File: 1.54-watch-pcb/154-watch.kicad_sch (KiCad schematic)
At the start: 59 parts, among them J1 AFC24-S24FIC-00, J2 Conn_01x06_Female, J3 USB_C_Programming, J4 Jack-DC, J5 Conn_01x02_Male, Q1 Si1308, Q2 BC817, Q3 BC817, Q4 Si2301CDS, SW1 RESET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

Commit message: RX -> TX  should be always crossed
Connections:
- net RX: now also U3.17 (RXD); no longer U3.18 (TXD)
- net TX: now also U3.18 (TXD); no longer U3.17 (RXD)
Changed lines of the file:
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@@
+    )
+  )
+  (global_label "TX" (shape input) (at 323.85 64.77 180) (fields_autoplaced)
+    (effects (font (size 1.27 1.27)) (justify right))
+    (property "Intersheet References" "${INTERSHEET_REFS}" (id 0) (at 319.2598 64.8494 0)
+      (effects (font (size 1.27 1.27)) (justify right) hide)
     )
   )
@@
     (effects (font (size 1.27 1.27)) (justify right))
     (property "Intersheet References" "${INTERSHEET_REFS}" (id 0) (at 158.2721 199.3106 0)
-      (effects (font (size 1.27 1.27)) (justify right) hide)
-    )
-  )
-  (global_label "RX" (shape input) (at 323.85 64.77 180) (fields_autoplaced)
-    (effects (font (size 1.27 1.27)) (justify right))
-    (property "Intersheet References" "${INTERSHEET_REFS}" (id 0) (at 318.9574 64.8494 0)
       (effects (font (size 1.27 1.27)) (justify right) hide)
     )
@@
     )
   )
-  (global_label "TX" (shape input) (at 328.93 67.31 180) (fields_autoplaced)
-    (effects (font (size 1.27 1.27)) (justify right))
-    (property "Intersheet References" "${INTERSHEET_REFS}" (id 0) (at 324.3398 67.3894 0)
+  (global_label "RX" (shape input) (at 328.93 67.31 180) (fields_autoplaced)
+    (effects (font (size 1.27 1.27)) (justify right))
+    (property "Intersheet References" "${INTERSHEET_REFS}" (id 0) (at 324.0374 67.3894 0)
       (effects (font (size 1.27 1.27)) (justify right) hide)
     )
@@
       (effects (font (size 1.27 1.27)) hide)
     )
-    (property "Value" "GND" (id 1) (at 355.6 57.15 0))
+    (property "Value" "GND" (id 1) (at 359.41 59.69 0))
     (property "Footprint" "" (id 2) (at 359.41 55.88 0)
       (effects (font (size 1.27 1.27)) hide)

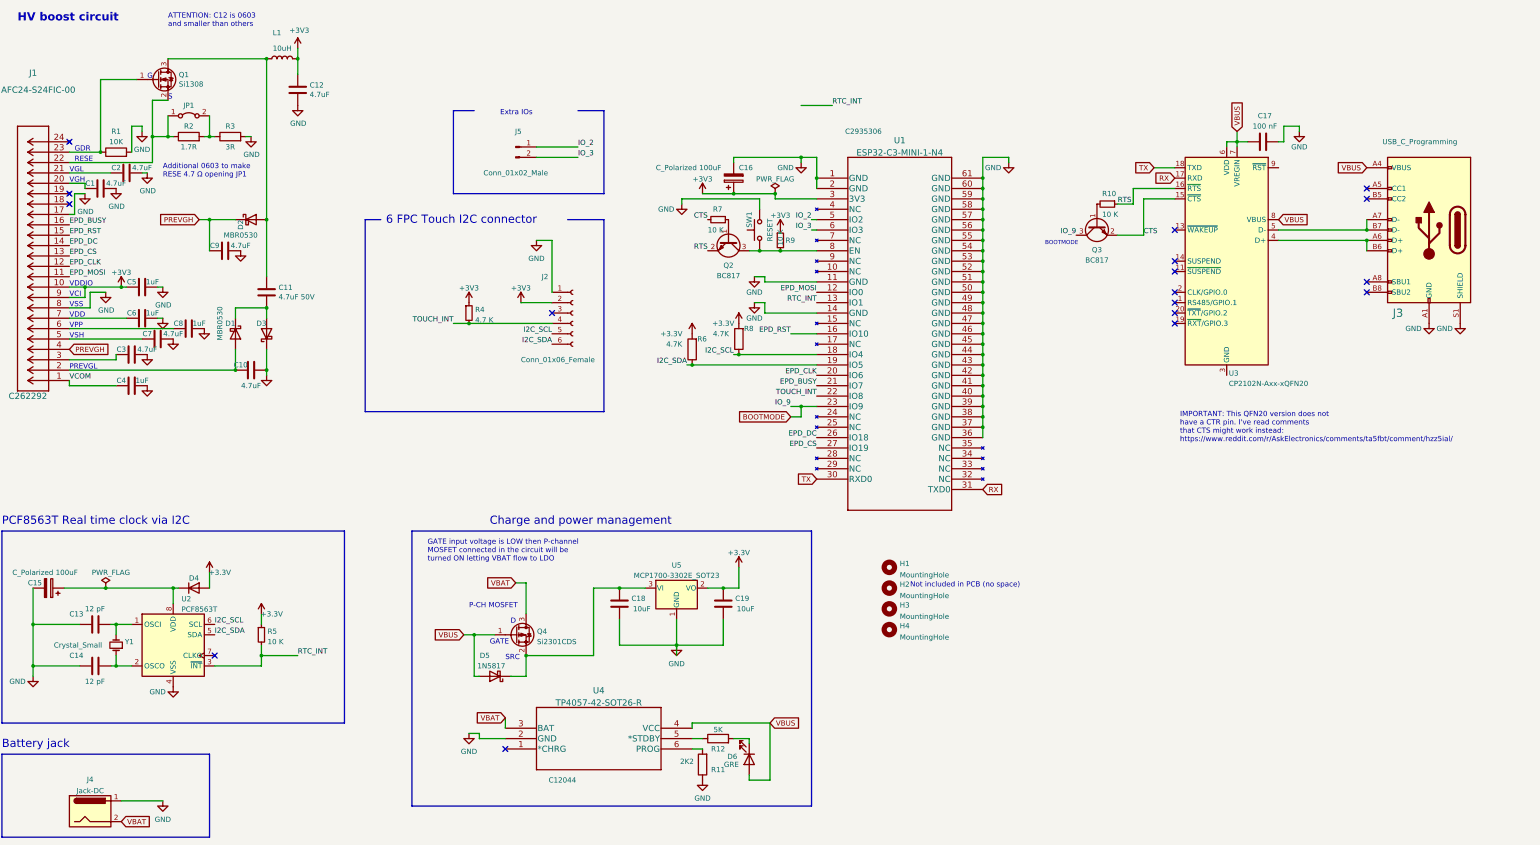
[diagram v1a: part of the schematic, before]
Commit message: #6 update 1.54" PCB to match sample sent by GOODISPLAY
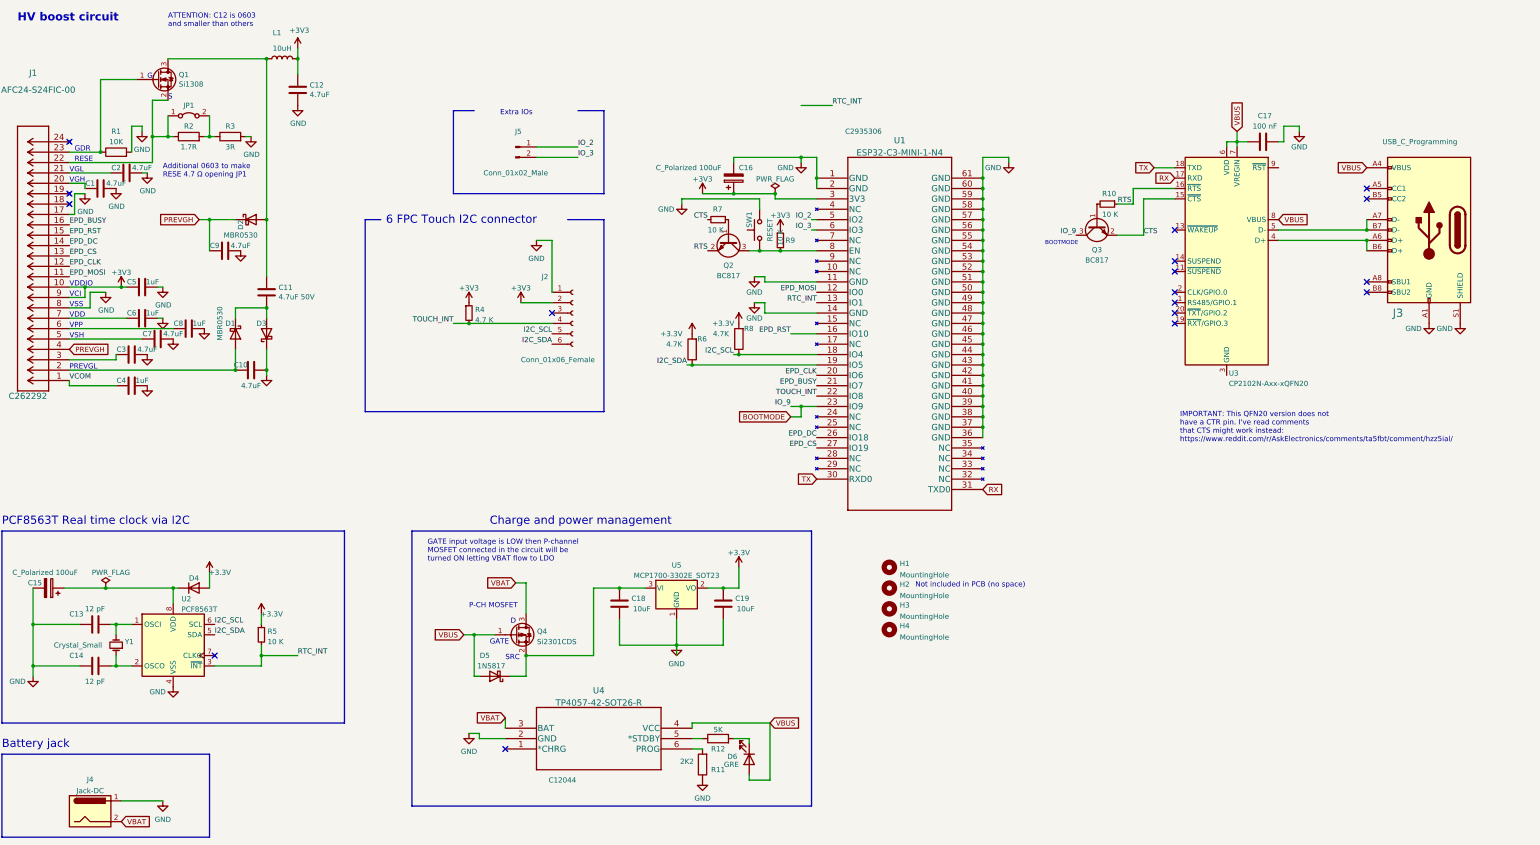
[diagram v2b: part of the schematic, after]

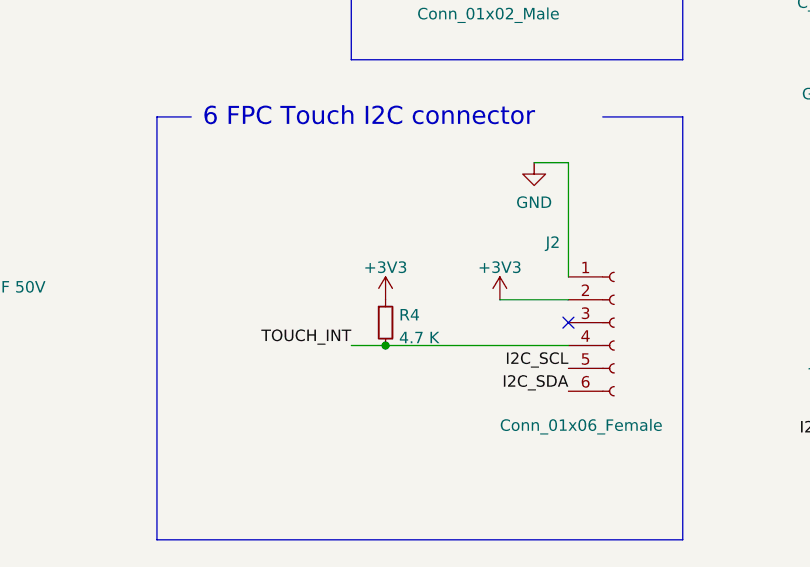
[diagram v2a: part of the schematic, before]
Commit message: #6 Update touch PINUP (Was wrong)
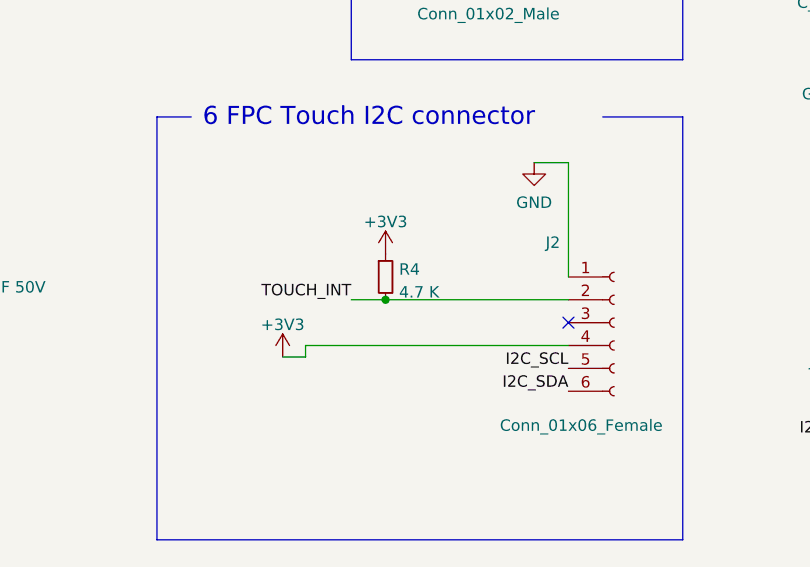
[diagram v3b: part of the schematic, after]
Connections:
- net +3V3: now also J2.4 (Pin_4); no longer J2.2 (Pin_2)
- net TOUCH_INT: now also J2.2 (Pin_2); no longer J2.4 (Pin_4)
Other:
- moved on the sheet: R4
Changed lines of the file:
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@@
   (junction (at 106.68 77.47) (diameter 0) (color 0 0 0 0)
   )
-  (junction (at 156.21 102.87) (diameter 0) (color 0 0 0 0)
-  )
   (junction (at 375.92 80.01) (diameter 0) (color 0 0 0 0)
   )
@@
   (junction (at 281.94 115.57) (diameter 0) (color 0 0 0 0)
   )
+  (junction (at 156.21 97.79) (diameter 0) (color 0 0 0 0)
+  )
   (no_connect (at 328.93 90.17))
   (no_connect (at 165.1 207.01))
@@
     (stroke (width 0) (type default))
   )
+  (wire (pts (xy 147.32 102.87) (xy 147.32 104.14))
+    (stroke (width 0) (type default))
+  )
   (polyline (pts (xy 41.91 153.67) (xy 41.91 200.66))
     (stroke (width 0) (type default))
@@
     (stroke (width 0) (type default))
   )
-  (wire (pts (xy 168.91 97.79) (xy 176.53 97.79))
-    (stroke (width 0) (type default))
-  )
   (wire (pts (xy 209.55 113.03) (xy 210.82 113.03))
     (stroke (width 0) (type default))
   )
-  (wire (pts (xy 156.21 102.87) (xy 176.53 102.87))
-    (stroke (width 0) (type default))
-  )
   (wire (pts (xy 375.92 82.55) (xy 375.92 85.09))
     (stroke (width 0) (type default))
@@
     (stroke (width 0) (type default))
   )
+  (wire (pts (xy 176.53 102.87) (xy 147.32 102.87))
+    (stroke (width 0) (type default))
+  )
   (wire (pts (xy 106.68 38.1) (xy 106.68 77.47))
     (stroke (width 0) (type default))
@@
     (stroke (width 0) (type default))
   )
-  (wire (pts (xy 152.4 102.87) (xy 156.21 102.87))
+  (wire (pts (xy 152.4 97.79) (xy 156.21 97.79))
     (stroke (width 0) (type default))
   )
@@
     (stroke (width 0) (type default))
   )
+  (wire (pts (xy 147.32 104.14) (xy 144.78 104.14))
+    (stroke (width 0) (type default))
+  )
   (wire (pts (xy 210.82 113.03) (xy 241.3 113.03))
     (stroke (width 0) (type default))
@@
     (stroke (width 0) (type default))
   )
+  (wire (pts (xy 156.21 97.79) (xy 176.53 97.79))
+    (stroke (width 0) (type default))
+  )
   (wire (pts (xy 210.82 200.66) (xy 210.82 201.93))
     (stroke (width 0) (type default))
@@
     (effects (font (size 1.27 1.27)) (justify left bottom))
   )
-  (label "TOUCH_INT" (at 152.4 102.87 180) (fields_autoplaced)
+  (label "TOUCH_INT" (at 152.4 97.79 180) (fields_autoplaced)
     (effects (font (size 1.27 1.27)) (justify right bottom))
   )
@@
     )
   )
-  (symbol (lib_id "power:+3V3") (at 168.91 97.79 0) (unit 1)
+  (symbol (lib_id "power:+3V3") (at 144.78 104.14 0) (unit 1)
     (in_bom yes) (on_board yes) (dnp no) (fields_autoplaced)
-    (property "Reference" "#PWR021" (at 168.91 101.6 0)
+    (property "Reference" "#PWR021" (at 144.78 107.95 0)
       (effects (font (size 1.27 1.27)) hide)
     )
-    (property "Value" "+3V3" (at 168.91 94.2142 0)
+    (property "Value" "+3V3" (at 144.78 100.5642 0)
       (effects (font (size 1.27 1.27)))
     )
-    (property "Footprint" "" (at 168.91 97.79 0)
+    (property "Footprint" "" (at 144.78 104.14 0)
       (effects (font (size 1.27 1.27)) hide)
     )
-    (property "Datasheet" "" (at 168.91 97.79 0)
+    (property "Datasheet" "" (at 144.78 104.14 0)
       (effects (font (size 1.27 1.27)) hide)
     )
@@
     )
   )
-  (symbol (lib_id "power:+3V3") (at 156.21 97.79 0) (unit 1)
+  (symbol (lib_id "power:+3V3") (at 156.21 92.71 0) (unit 1)
     (in_bom yes) (on_board yes) (dnp no) (fields_autoplaced)
-    (property "Reference" "#PWR05" (at 156.21 101.6 0)
+    (property "Reference" "#PWR05" (at 156.21 96.52 0)
       (effects (font (size 1.27 1.27)) hide)
     )
-    (property "Value" "+3V3" (at 156.21 94.2142 0)
+    (property "Value" "+3V3" (at 156.21 89.1342 0)
       (effects (font (size 1.27 1.27)))
     )
-    (property "Footprint" "" (at 156.21 97.79 0)
+    (property "Footprint" "" (at 156.21 92.71 0)
       (effects (font (size 1.27 1.27)) hide)
     )
-    (property "Datasheet" "" (at 156.21 97.79 0)
+    (property "Datasheet" "" (at 156.21 92.71 0)
       (effects (font (size 1.27 1.27)) hide)
     )
@@
     )
   )
-  (symbol (lib_id "Device:R_Small") (at 156.21 100.33 0) (unit 1)
+  (symbol (lib_id "Device:R_Small") (at 156.21 95.25 0) (unit 1)
     (in_bom yes) (on_board yes) (dnp no)
-    (property "Reference" "R4" (at 157.7086 99.4953 0)
+    (property "Reference" "R4" (at 157.7086 94.4153 0)
       (effects (font (size 1.27 1.27)) (justify left))
     )
-    (property "Value" "4.7 K" (at 157.7086 102.0322 0)
+    (property "Value" "4.7 K" (at 157.7086 96.9522 0)
       (effects (font (size 1.27 1.27)) (justify left))
     )
-    (property "Footprint" "Resistor_SMD:R_0603_1608Metric" (at 156.21 100.33 0)
+    (property "Footprint" "Resistor_SMD:R_0603_1608Metric" (at 156.21 95.25 0)
       (effects (font (size 1.27 1.27)) hide)
     )
-    (property "Datasheet" "https://jlcpcb.com/partdetail/23889-0603WAF4701T5E/C23162" (at 156.21 100.33 0)
+    (property "Datasheet" "https://jlcpcb.com/partdetail/23889-0603WAF4701T5E/C23162" (at 156.21 95.25 0)
       (effects (font (size 1.27 1.27)) hide)
     )
-    (property "LCSC" "C23162" (at 156.21 100.33 0)
+    (property "LCSC" "C23162" (at 156.21 95.25 0)
       (effects (font (size 1.27 1.27)) hide)
     )

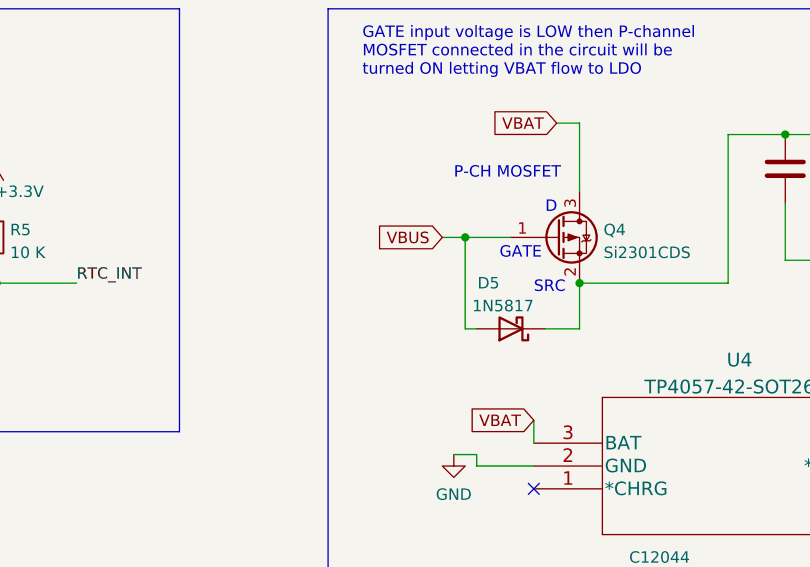
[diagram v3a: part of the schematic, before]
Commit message: #6 Add a pull-down to power switch Q4
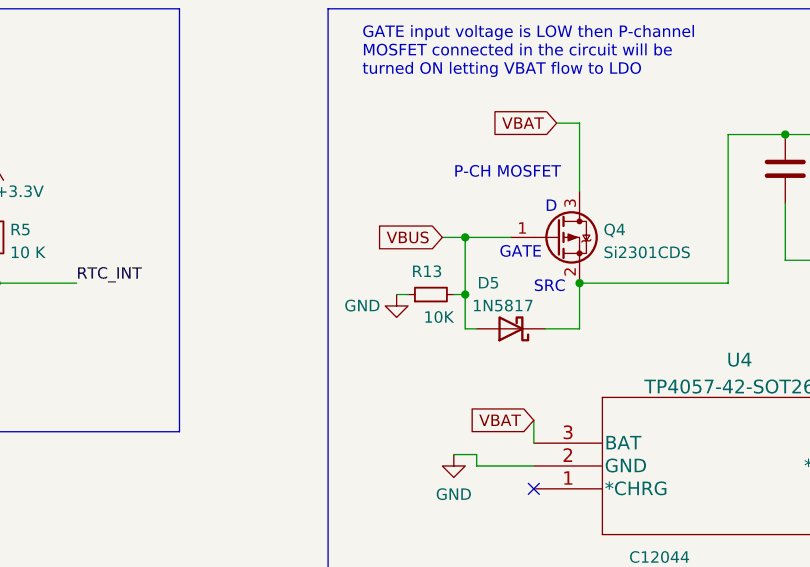
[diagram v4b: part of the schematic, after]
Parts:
- added R13: 10K, Resistor_SMD:R_0603_1608Metric, symbol Device:R_Small
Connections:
- net GND: now also R13.1
- net VBUS: now also R13.2
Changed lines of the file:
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@@
   (junction (at 281.94 100.33) (diameter 0) (color 0 0 0 0)
   )
+  (junction (at 157.48 185.42) (diameter 0) (color 0 0 0 0)
+  )
   (junction (at 71.12 93.98) (diameter 0) (color 0 0 0 0)
   )
@@
     (stroke (width 0) (type default))
   )
+  (wire (pts (xy 156.21 185.42) (xy 157.48 185.42))
+    (stroke (width 0) (type default))
+  )
   (wire (pts (xy 228.6 92.71) (xy 228.6 91.44))
     (stroke (width 0) (type default))
@@
     (stroke (width 0) (type default))
   )
-  (wire (pts (xy 157.48 179.07) (xy 157.48 189.23))
+  (wire (pts (xy 157.48 179.07) (xy 157.48 185.42))
     (stroke (width 0) (type default))
   )
@@
     (stroke (width 0) (type default))
   )
+  (wire (pts (xy 149.86 185.42) (xy 151.13 185.42))
+    (stroke (width 0) (type default))
+  )
   (wire (pts (xy 227.33 74.93) (xy 227.33 72.39))
     (stroke (width 0) (type default))
@@
     (stroke (width 0) (type default))
   )
+  (wire (pts (xy 157.48 185.42) (xy 157.48 189.23))
+    (stroke (width 0) (type default))
+  )
   (wire (pts (xy 359.41 54.61) (xy 359.41 55.88))
     (stroke (width 0) (type default))
@@
     )
   )
+  (symbol (lib_id "power:GND") (at 149.86 185.42 0) (unit 1)
+    (in_bom yes) (on_board yes) (dnp no)
+    (property "Reference" "#PWR034" (at 149.86 191.77 0)
+      (effects (font (size 1.27 1.27)) hide)
+    )
+    (property "Value" "GND" (at 146.05 186.69 0)
+      (effects (font (size 1.27 1.27)))
+    )
+    (property "Footprint" "" (at 149.86 185.42 0)
+      (effects (font (size 1.27 1.27)) hide)
+    )
+    (property "Datasheet" "" (at 149.86 185.42 0)
+      (effects (font (size 1.27 1.27)) hide)
+    )
+    (pin "1")
+    (instances
+      (project "154-watch"
+        (path "/ea6fde00-59dc-4a79-a647-7e38199fae0e"
+          (reference "#PWR034") (unit 1)
+        )
+      )
+    )
+  )
   (symbol (lib_id "power:GND") (at 77.47 110.49 0) (unit 1)
     (in_bom yes) (on_board yes) (dnp no)
@@
         )
       )
+    )
+  )
+  (symbol (lib_id "Device:R_Small") (at 153.67 185.42 90) (unit 1)
+    (in_bom yes) (on_board yes) (dnp no)
+    (property "Reference" "R13" (at 154.94 182.88 90)
+      (effects (font (size 1.27 1.27)) (justify left))
+    )
+    (property "Value" "10K" (at 156.21 187.96 90)
+      (effects (font (size 1.27 1.27)) (justify left))
+    )
+    (property "Footprint" "Resistor_SMD:R_0603_1608Metric" (at 153.67 185.42 0)
+      (effects (font (size 1.27 1.27)) hide)
+    )
+    (property "Datasheet" "https://datasheet.lcsc.com/lcsc/2206010045_UNI-ROYAL-Uniroyal-Elec-0603WAF1002T5E_C25804.pdf" (at 153.67 185.42 0)
+      (effects (font (size 1.27 1.27)) hide)
+    )
+    (property "LCSC" "C25804" (at 153.67 185.42 90)
+      (effects (font (size 1.27 1.27)) hide)
+    )
+    (pin "1")
+    (pin "2")
+    (instances
+      (project "154-watch"
+        (path "/ea6fde00-59dc-4a79-a647-7e38199fae0e"
+          (reference "R13") (unit 1)
+        )
+      )
